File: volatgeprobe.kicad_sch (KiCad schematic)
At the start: 52 parts, among them IC1 AMC1301SDWV, J1 Conn_01x01_Male, J2 Conn_01x01_Male, J3 Conn_01x02_Male, J4 Conn_Coaxial, SW1 SW_SPST, U1 AZ1117IH-3.3TRG1, U2 5-15v, U4 LF353M, U5 LF353M

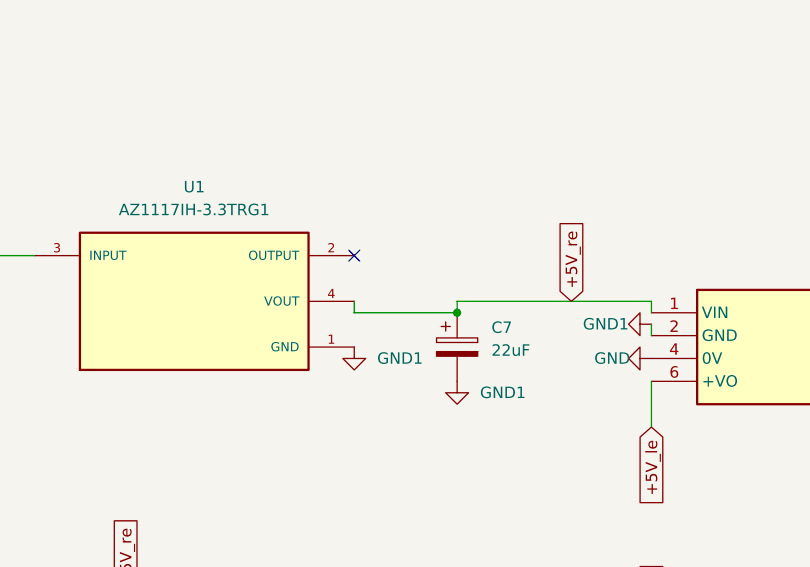
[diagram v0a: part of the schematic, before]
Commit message: shorted ldo outs
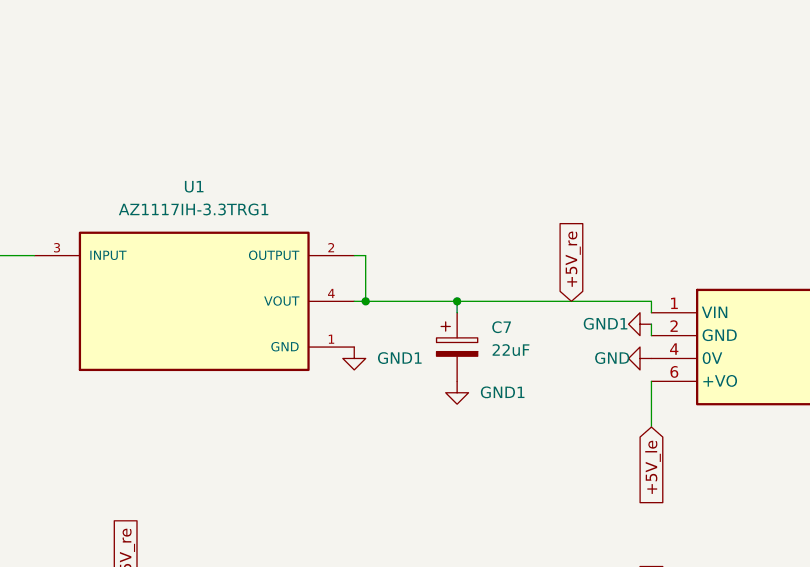
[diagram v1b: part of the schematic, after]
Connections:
- net +5V_re: now also U1.2 (OUTPUT)
- no-connect marks 1 -> 0
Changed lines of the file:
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@@
   (junction (at 110.49 134.62) (diameter 0) (color 0 0 0 0)
   )
+  (junction (at 92.71 196.85) (diameter 0) (color 0 0 0 0)
+  )
   (junction (at 236.22 144.78) (diameter 0) (color 0 0 0 0)
   )
@@
   (junction (at 118.11 132.08) (diameter 0) (color 0 0 0 0)
   )
-  (junction (at 102.87 198.12) (diameter 0) (color 0 0 0 0)
+  (junction (at 102.87 196.85) (diameter 0) (color 0 0 0 0)
   )
   (junction (at 259.08 208.28) (diameter 0) (color 0 0 0 0)
@@
   (junction (at 116.84 120.65) (diameter 0) (color 0 0 0 0)
   )
-  (no_connect (at 91.44 191.77))
   (wire (pts (xy 153.67 114.3) (xy 167.64 114.3))
     (stroke (width 0) (type default))
@@
     (stroke (width 0) (type default))
   )
-  (wire (pts (xy 91.44 198.12) (xy 91.44 196.85))
-    (stroke (width 0) (type default))
-  )
   (wire (pts (xy 185.42 199.39) (xy 186.69 199.39))
     (stroke (width 0) (type default))
@@
     (stroke (width 0) (type default))
   )
+  (wire (pts (xy 92.71 196.85) (xy 102.87 196.85))
+    (stroke (width 0) (type default))
+  )
   (wire (pts (xy 120.65 138.43) (xy 119.38 138.43))
     (stroke (width 0) (type default))
@@
     (stroke (width 0) (type default))
   )
-  (wire (pts (xy 91.44 198.12) (xy 102.87 198.12))
+  (wire (pts (xy 91.44 196.85) (xy 92.71 196.85))
     (stroke (width 0) (type default))
   )
@@
     (stroke (width 0) (type default))
   )
+  (wire (pts (xy 91.44 191.77) (xy 92.71 191.77))
+    (stroke (width 0) (type default))
+  )
   (wire (pts (xy 176.53 146.05) (xy 176.53 151.13))
     (stroke (width 0) (type default))
@@
     (stroke (width 0) (type default))
   )
+  (wire (pts (xy 92.71 196.85) (xy 92.71 191.77))
+    (stroke (width 0) (type default))
+  )

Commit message: inductors foot print changed
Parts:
- L1, L2: footprint inductor:INDM7676X435N -> inductor:DR74
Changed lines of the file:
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@@
       (effects (font (size 1.27 1.27)))
     )
-    (property "Footprint" "inductor:INDM7676X435N" (at 241.3 200.66 0)
+    (property "Footprint" "inductor:DR74" (at 241.3 200.66 0)
       (effects (font (size 1.27 1.27)) hide)
     )
@@
       (effects (font (size 1.27 1.27)))
     )
-    (property "Footprint" "inductor:INDM7676X435N" (at 179.07 199.39 0)
+    (property "Footprint" "inductor:DR74" (at 179.07 199.39 0)
       (effects (font (size 1.27 1.27)) hide)
     )
